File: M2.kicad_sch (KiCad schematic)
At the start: 1 part

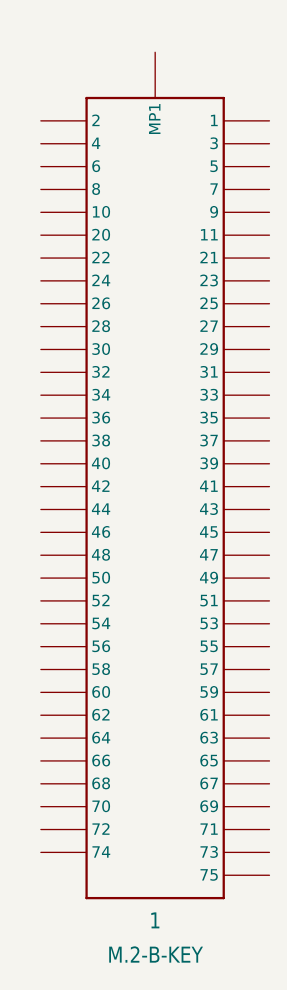
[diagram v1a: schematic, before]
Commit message: ADD : Footprint assignment. FIX : Various ERC rules.
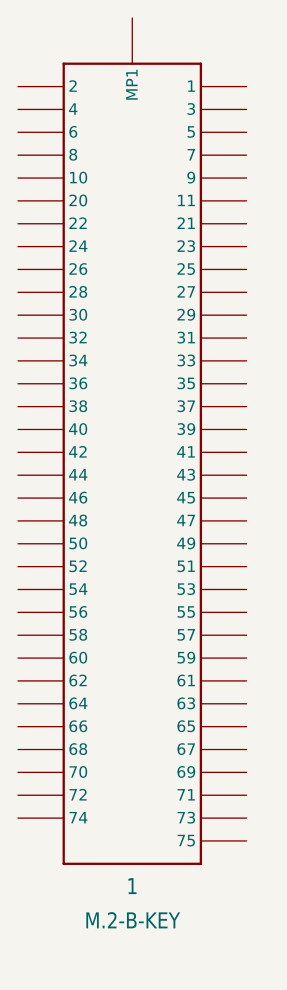
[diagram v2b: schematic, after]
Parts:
- 1: footprint (none) -> M.2-Templates:M.2-B-KEY
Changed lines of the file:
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@@
 	(symbol
 		(lib_id "M.2-Templates-eagle-import:M.2-B-KEY")
-		(at 138.43 146.05 0)
+		(at 135.89 142.24 0)
 		(unit 1)
 		(exclude_from_sim no)
@@
 		(fields_autoplaced yes)
 		(property "Reference" "1"
-			(at 146.05 148.59 0)
+			(at 143.51 144.78 0)
 			(effects
 				(font
@@
 		)
 		(property "Value" "M.2-B-KEY"
-			(at 146.05 152.4 0)
+			(at 143.51 148.59 0)
 			(effects
 				(font
@@
 			)
 		)
-		(property "Footprint" ""
-			(at 138.43 146.05 0)
+		(property "Footprint" "M.2-Templates:M.2-B-KEY"
+			(at 135.89 142.24 0)
 			(effects
 				(font
@@
 		)
 		(property "Datasheet" ""
-			(at 138.43 146.05 0)
+			(at 135.89 142.24 0)
 			(effects
 				(font
@@
 		)
 		(property "Description" ""
-			(at 138.43 146.05 0)
+			(at 135.89 142.24 0)
 			(effects
 				(font
@@
 			)
 		)
-		(pin "P$64"
+		(pin "P$1"
+		)
+		(pin "P$11"
+		)
+		(pin "P$40"
+		)
+		(pin "P$42"
+		)
+		(pin "P$28"
+		)
+		(pin "P$52"
+		)
+		(pin "P$41"
+		)
+		(pin "P$68"
+		)
+		(pin "P$31"
+		)
+		(pin "P$50"
+		)
+		(pin "P$33"
+		)
+		(pin "P$45"
+		)
+		(pin "P$49"
 		)
 		(pin "P$66"
 		)
-		(pin "P$45"
+		(pin "P$55"
+		)
+		(pin "P$26"
+		)
+		(pin "P$58"
+		)
+		(pin "P$60"
+		)
+		(pin "P$9"
+		)
+		(pin "P$34"
+		)
+		(pin "P$48"
+		)
+		(pin "P$57"
+		)
+		(pin "P$4"
+		)
+		(pin "P$46"
+		)
+		(pin "P$6"
+		)
+		(pin "P$74"
+		)
+		(pin "P$20"
+		)
+		(pin "P$70"
+		)
+		(pin "P$3"
+		)
+		(pin "P$7"
+		)
+		(pin "P$25"
+		)
+		(pin "P$2"
+		)
+		(pin "P$10"
+		)
+		(pin "P$22"
+		)
+		(pin "P$44"
+		)
+		(pin "P$64"
+		)
+		(pin "P$8"
+		)
+		(pin "P$27"
+		)
+		(pin "P$36"
+		)
+		(pin "P$35"
+		)
+		(pin "P$24"
+		)
+		(pin "P$30"
+		)
+		(pin "P$54"
+		)
+		(pin "P$56"
+		)
+		(pin "P$72"
+		)
+		(pin "P$38"
+		)
+		(pin "P$32"
+		)
+		(pin "MOUNTING-HOLE"
+		)
+		(pin "P$62"
+		)
+		(pin "P$5"
+		)
+		(pin "P$21"
+		)
+		(pin "P$29"
+		)
+		(pin "P$23"
+		)
+		(pin "P$37"
+		)
+		(pin "P$39"
+		)
+		(pin "P$43"
+		)
+		(pin "P$51"
 		)
 		(pin "P$47"
 		)
+		(pin "P$53"
+		)
 		(pin "P$63"
 		)
-		(pin "P$23"
+		(pin "P$75"
 		)
-		(pin "P$38"
+		(pin "P$69"
 		)
-		(pin "P$39"
+		(pin "P$73"
 		)
-		(pin "P$27"
-		)
-		(pin "P$48"
-		)
-		(pin "P$7"
-		)
-		(pin "P$70"
-		)
-		(pin "P$29"
-		)
-		(pin "P$43"
-		)
-		(pin "P$33"
-		)
-		(pin "P$54"
-		)
-		(pin "P$31"
-		)
-		(pin "P$62"
-		)
-		(pin "P$57"
-		)
-		(pin "P$42"
-		)
-		(pin "P$4"
+		(pin "P$67"
 		)
 		(pin "P$59"
 		)
-		(pin "P$32"
+		(pin "P$71"
 		)
-		(pin "P$44"
-		)
-		(pin "P$35"
-		)
-		(pin "P$41"
-		)
-		(pin "P$2"
-		)
-		(pin "P$53"
-		)
-		(pin "P$49"
-		)
-		(pin "P$6"
+		(pin "P$61"
 		)
 		(pin "P$65"
 		)
-		(pin "P$67"
-		)
-		(pin "P$68"
-		)
-		(pin "P$51"
-		)
-		(pin "P$36"
-		)
-		(pin "P$22"
-		)
-		(pin "P$40"
-		)
-		(pin "P$25"
-		)
-		(pin "P$60"
-		)
-		(pin "P$52"
-		)
-		(pin "P$69"
-		)
-		(pin "P$28"
-		)
-		(pin "P$1"
-		)
-		(pin "P$20"
-		)
-		(pin "P$46"
-		)
-		(pin "P$34"
-		)
-		(pin "P$10"
-		)
-		(pin "P$56"
-		)
-		(pin "P$11"
-		)
-		(pin "P$24"
-		)
-		(pin "P$58"
-		)
-		(pin "P$30"
-		)
-		(pin "P$55"
-		)
-		(pin "P$21"
-		)
-		(pin "P$37"
-		)
-		(pin "P$26"
-		)
-		(pin "P$3"
-		)
-		(pin "MOUNTING-HOLE"
-		)
-		(pin "P$50"
-		)
-		(pin "P$61"
-		)
-		(pin "P$5"
-		)
-		(pin "P$72"
-		)
-		(pin "P$8"
-		)
-		(pin "P$9"
-		)
-		(pin "P$71"
-		)
-		(pin "P$75"
-		)
-		(pin "P$73"
-		)
-		(pin "P$74"
-		)
 		(instances
-			(project "STMBlueLine"
+			(project ""
 				(path "/d9f70aa0-fcfd-4ae4-9801-1024ce5b770a/666ee3ec-a1ed-4703-98a8-cdaea5f84fb1"
 					(reference "1")
